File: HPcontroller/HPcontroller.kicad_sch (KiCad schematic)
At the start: 35 parts, among them Q1 Q_Dual_NMOS_S1G1S2G2D2D2D1D1, U1 Adafruit_QTPY_ESP32-C3, U2 NCP81071B, U5 ER-OLED0.49-1_MODULE, U6 Adafruit_MAX31850, U7 Adafruit_QTPY_ESP32-C3

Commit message: design "finished" need to do bom and footprints and layout
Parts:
- removed C1: 10u, Capacitor_SMD:C_0805_2012Metric_Pad1.18x1.45mm_HandSolder, symbol Device:C
- removed C4: C, Capacitor_SMD:C_0805_2012Metric_Pad1.18x1.45mm_HandSolder, symbol Device:C
- removed D1: D, Diode_SMD:D_SMB_Handsoldering, symbol Device:D
- removed D_3V3_POW1, D_HEAT1, D_HOT1, D_PD_POW1, D_RUN1: LED, LED_SMD:LED_0603_1608Metric_Pad1.05x0.95mm_HandSolder, symbol Device:LED
- removed Q1: Q_Dual_NMOS_S1G1S2G2D2D2D1D1, Package_SO:SOIC-8_3.9x4.9mm_P1.27mm, symbol Device:Q_Dual_NMOS_S1G1S2G2D2D2D1D1
- removed R1, R5, R6, R8: 100, Resistor_SMD:R_0805_2012Metric_Pad1.20x1.40mm_HandSolder, symbol Device:R
- removed R10, R7: 10k, Resistor_SMD:R_0805_2012Metric_Pad1.20x1.40mm_HandSolder, symbol Device:R
- removed R11: R, connector_custom:AMASS_XT60PW-M, symbol Device:R
- removed R14: 4k7, Resistor_SMD:R_0805_2012Metric_Pad1.20x1.40mm_HandSolder, symbol Device:R
- removed R4: 1k5, Resistor_SMD:R_0805_2012Metric_Pad1.20x1.40mm_HandSolder, symbol Device:R
- removed R9: 0, Jumper:SolderJumper-2_P1.3mm_Bridged_RoundedPad1.0x1.5mm, symbol Device:R
- removed SWDEC1, SWINC1, SWRST1, SWRUN1: SW_SPST, Button_Switch_SMD:SW_SPST_PTS645, symbol Switch:SW_SPST
- removed SWMODE1: SW_SPDT, Button_Switch_THT:SW_Slide_1P2T_CK_OS102011MS2Q, symbol Switch:SW_SPDT
- removed U1: Adafruit_QTPY_ESP32-C3, DevBoards:QTPY ESP32 C3, symbol DevBoards:Adafruit_QTPY_ESP32-C3
- removed U2: NCP81071B, Package_SO:SOIC-8_3.9x4.9mm_P1.27mm, symbol project_assorted:NCP81071B
- removed U5: ER-OLED0.49-1_MODULE, Connector_PinSocket_2.54mm:PinSocket_1x04_P2.54mm_Vertical, symbol DevBoards:ER-OLED0.49-1_MODULE
- removed U6: Adafruit_MAX31850, Connector_PinSocket_2.54mm:PinSocket_1x08_P2.54mm_Vertical, symbol DevBoards:Adafruit_MAX31850
- added J1: AudioJack4_Ground, symbol Connector_Audio:AudioJack4_Ground
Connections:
- net +3V3: now also J1.R2
- net GND: now also J1.S
- net SCL: now also U7.6 (SCL), J1.R1
- net SDA: now also U7.5 (SDA), J1.T
- net HEAT_DRIVE: now reaches U7.1 (A0)
- net SEL_A: now reaches U7.3 (A2)
- net SEL_B: now reaches U7.4 (A3)
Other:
- added sheet Controlpad (Controlpad.kicad_sch)
- added sheet Temperature Measurement System (Tmeas.kicad_sch)
- sheet HEATER DRIVE ports: added ENABLE_HEATER_DRIVE, HEATER FET DRIVE; removed none
- sheet ThermalProtector ports: added none; removed THM_PROT_RES
- note removed: "R11 is an xt60 to another board"
- moved on the sheet: H1, H2, H3, H4, R2, R3, U7

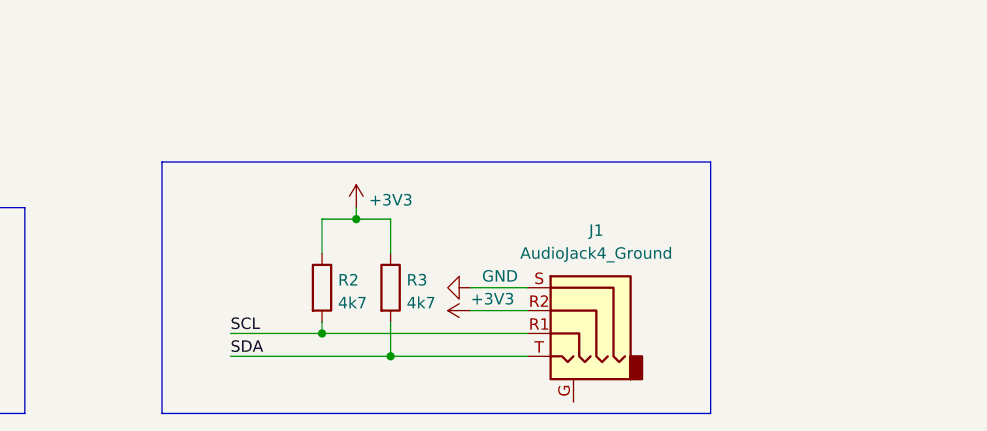
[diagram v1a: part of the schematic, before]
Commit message: started routing, finished footprintns
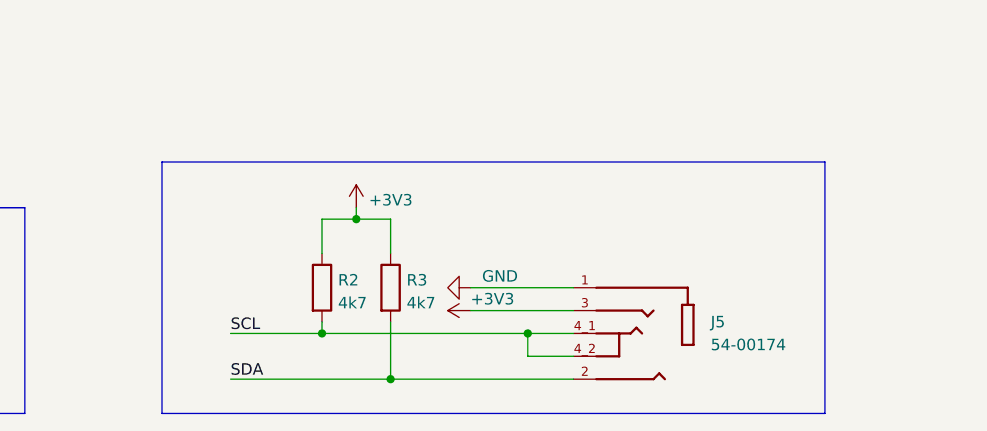
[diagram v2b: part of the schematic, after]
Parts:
- removed J1: AudioJack4_Ground, symbol Connector_Audio:AudioJack4_Ground
- added J5: 54-00174, TENSILITY_54-00174, symbol HPsym:54-00174
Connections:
- net +3V3: now also J5.3
- net GND: now also J5.1
- net SCL: now also J5.4_1, J5.4_2
- net SDA: now also J5.2
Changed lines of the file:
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@@
   (junction (at 105.41 171.45) (diameter 0) (color 0 0 0 0)
   )
-  (junction (at 109.22 186.69) (diameter 0) (color 0 0 0 0)
+  (junction (at 109.22 189.23) (diameter 0) (color 0 0 0 0)
+  )
+  (junction (at 124.46 184.15) (diameter 0) (color 0 0 0 0)
   )
   (junction (at 101.6 184.15) (diameter 0) (color 0 0 0 0)
@@
     (stroke (width 0) (type default))
   )
-  (wire (pts (xy 124.46 179.07) (xy 118.11 179.07))
+  (wire (pts (xy 118.11 179.07) (xy 129.54 179.07))
     (stroke (width 0) (type default))
   )
@@
     (stroke (width 0) (type default))
   )
+  (wire (pts (xy 124.46 186.69) (xy 124.46 184.15))
+    (stroke (width 0) (type default))
+  )
   (polyline (pts (xy 83.82 165.1) (xy 83.82 193.04))
     (stroke (width 0) (type default))
@@
     (stroke (width 0) (type default))
   )
+  (wire (pts (xy 124.46 184.15) (xy 129.54 184.15))
+    (stroke (width 0) (type default))
+  )
   (wire (pts (xy 101.6 175.26) (xy 101.6 171.45))
     (stroke (width 0) (type default))
   )
-  (wire (pts (xy 109.22 182.88) (xy 109.22 186.69))
-    (stroke (width 0) (type default))
-  )
   (polyline (pts (xy 68.58 193.04) (xy 21.59 193.04))
     (stroke (width 0) (type default))
@@
     (stroke (width 0) (type default))
   )
-  (wire (pts (xy 91.44 186.69) (xy 109.22 186.69))
-    (stroke (width 0) (type default))
-  )
-  (polyline (pts (xy 144.78 193.04) (xy 144.78 165.1))
+  (wire (pts (xy 91.44 189.23) (xy 109.22 189.23))
+    (stroke (width 0) (type default))
+  )
+  (polyline (pts (xy 157.48 193.04) (xy 157.48 165.1))
     (stroke (width 0) (type default))
   )
@@
     (stroke (width 0) (type default))
   )
-  (wire (pts (xy 109.22 186.69) (xy 124.46 186.69))
-    (stroke (width 0) (type default))
-  )
-  (polyline (pts (xy 83.82 165.1) (xy 144.78 165.1))
+  (wire (pts (xy 109.22 189.23) (xy 129.54 189.23))
+    (stroke (width 0) (type default))
+  )
+  (polyline (pts (xy 83.82 165.1) (xy 157.48 165.1))
     (stroke (width 0) (type default))
   )
@@
     (stroke (width 0) (type default))
   )
+  (wire (pts (xy 109.22 182.88) (xy 109.22 189.23))
+    (stroke (width 0) (type default))
+  )
   (wire (pts (xy 33.02 105.41) (xy 40.64 105.41))
     (stroke (width 0) (type default))
   )
-  (polyline (pts (xy 83.82 193.04) (xy 144.78 193.04))
+  (polyline (pts (xy 83.82 193.04) (xy 157.48 193.04))
+    (stroke (width 0) (type default))
+  )
+  (wire (pts (xy 129.54 186.69) (xy 124.46 186.69))
     (stroke (width 0) (type default))
   )
@@
     (stroke (width 0) (type default))
   )
-  (wire (pts (xy 118.11 181.61) (xy 124.46 181.61))
+  (wire (pts (xy 118.11 181.61) (xy 129.54 181.61))
     (stroke (width 0) (type default))
   )
@@
     (effects (font (size 1.27 1.27)) (justify left bottom))
   )
-  (label "SDA" (at 91.44 186.69 0) (fields_autoplaced)
+  (label "SDA" (at 91.44 189.23 0) (fields_autoplaced)
     (effects (font (size 1.27 1.27)) (justify left bottom))
   )
@@
         (path "/e63e39d7-6ac0-4ffd-8aa3-1841a4541b55"
           (reference "R2") (unit 1)
+        )
+      )
+    )
+  )
+  (symbol (lib_id "HPsym:54-00174") (at 137.16 184.15 0) (mirror y) (unit 1)
+    (in_bom yes) (on_board yes) (dnp no) (fields_autoplaced)
+    (property "Reference" "J5" (at 144.78 182.88 0)
+      (effects (font (size 1.27 1.27)) (justify right))
+    )
+    (property "Value" "54-00174" (at 144.78 185.42 0)
+      (effects (font (size 1.27 1.27)) (justify right))
+    )
+    (property "Footprint" "TENSILITY_54-00174" (at 138.43 173.99 0)
+      (effects (font (size 1.27 1.27)) (justify left bottom) hide)
+    )
+    (property "Datasheet" "" (at 137.16 184.15 0)
+      (effects (font (size 1.27 1.27)) (justify left bottom) hide)
+    )
+    (property "PARTREV" "A" (at 123.19 180.34 0)
+      (effects (font (size 1.27 1.27)) (justify left bottom) hide)
+    )
+    (property "STANDARD" "Manufacturer Recommendations" (at 138.43 176.53 0)
+      (effects (font (size 1.27 1.27)) (justify left bottom) hide)
+    )
+    (property "SNAPEDA_PN" "54-00174" (at 118.11 173.99 0)
+      (effects (font (size 1.27 1.27)) (justify left bottom) hide)
+    )
+    (property "MAXIMUM_PACKAGE_HEIGHT" "6mm" (at 121.92 180.34 0)
+      (effects (font (size 1.27 1.27)) (justify left bottom) hide)
+    )
+    (property "MANUFACTURER" "TENSILITY" (at 120.65 182.88 0)
+      (effects (font (size 1.27 1.27)) (justify left bottom) hide)
+    )
+    (property "MPN" "54-00174" (at 137.16 184.15 0)
+      (effects (font (size 1.27 1.27)) hide)
+    )
+    (pin "1")
+    (pin "2")
+    (pin "3")
+    (pin "4_1")
+    (pin "4_2")
+    (instances
+      (project "HPcontroller"
+        (path "/e63e39d7-6ac0-4ffd-8aa3-1841a4541b55"
+          (reference "J5") (unit 1)
         )
       )
@@
         )
       )
-    )
-  )
-  (symbol (lib_id "Connector_Audio:AudioJack4_Ground") (at 129.54 181.61 0) (mirror y) (unit 1)
-    (in_bom yes) (on_board yes) (dnp no)
-    (property "Reference" "J1" (at 132.08 172.72 0)
-      (effects (font (size 1.27 1.27)))
-    )
-    (property "Value" "AudioJack4_Ground" (at 132.08 175.26 0)
-      (effects (font (size 1.27 1.27)))
-    )
-    (property "Footprint" "" (at 129.54 181.61 0)
-      (effects (font (size 1.27 1.27)) hide)
-    )
-    (property "Datasheet" "~" (at 129.54 181.61 0)
-      (effects (font (size 1.27 1.27)) hide)
-    )
-    (pin "G")
-    (pin "R1")
-    (pin "R2")
-    (pin "S")
-    (pin "T")
-    (instances
-      (project "HPcontroller"
-        (path "/e63e39d7-6ac0-4ffd-8aa3-1841a4541b55"
-          (reference "J1") (unit 1)
-        )
-      )

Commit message: finished routing, moving on to heater
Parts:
- H1, H2, H3, H4: footprint MountingHole:MountingHole_3.2mm_M3_ISO14580 -> MountingHole:MountingHole_2.7mm_M2.5
- U7: footprint DevBoards:QTPY ESP32 C3 -> HPfootprint:QTPY ESP32 C3
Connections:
- net +3V3: now also U7.12 (3v3)
- net GND: now also U7.13 (GND)
- net SEL_A: now also U7.4 (A3); no longer U7.3 (A2)
- net SEL_B: now also U7.3 (A2); no longer U7.4 (A3)
- net INTA: now reaches U7.10 (MISO)
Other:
- sheet Controlpad ports: added INTA, SCL, SDA; removed none
- moved on the sheet: U7
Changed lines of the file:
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@@
+    (stroke (width 0) (type default))
+  )
+  (wire (pts (xy 53.34 105.41) (xy 59.69 105.41))
     (stroke (width 0) (type default))
   )
@@
     (stroke (width 0) (type default))
   )
-  (wire (pts (xy 33.02 102.87) (xy 40.64 102.87))
+  (wire (pts (xy 22.86 107.95) (xy 30.48 107.95))
     (stroke (width 0) (type default))
   )
@@
     (stroke (width 0) (type default))
   )
-  (wire (pts (xy 26.67 97.79) (xy 40.64 97.79))
+  (wire (pts (xy 16.51 102.87) (xy 30.48 102.87))
     (stroke (width 0) (type default))
   )
@@
     (stroke (width 0) (type default))
   )
+  (wire (pts (xy 171.45 101.6) (xy 177.8 101.6))
+    (stroke (width 0) (type default))
+  )
   (polyline (pts (xy 68.58 193.04) (xy 21.59 193.04))
     (stroke (width 0) (type default))
   )
+  (wire (pts (xy 171.45 99.06) (xy 177.8 99.06))
+    (stroke (width 0) (type default))
+  )
   (wire (pts (xy 87.63 139.7) (xy 93.98 139.7))
     (stroke (width 0) (type default))
@@
     (stroke (width 0) (type default))
   )
+  (wire (pts (xy 53.34 113.03) (xy 60.96 113.03))
+    (stroke (width 0) (type default))
+  )
   (wire (pts (xy 80.01 115.57) (xy 93.98 115.57))
     (stroke (width 0) (type default))
@@
     (stroke (width 0) (type default))
   )
-  (wire (pts (xy 33.02 105.41) (xy 40.64 105.41))
+  (wire (pts (xy 22.86 110.49) (xy 30.48 110.49))
     (stroke (width 0) (type default))
   )
@@
     (stroke (width 0) (type default))
   )
+  (wire (pts (xy 171.45 104.14) (xy 177.8 104.14))
+    (stroke (width 0) (type default))
+  )
   (wire (pts (xy 129.54 186.69) (xy 124.46 186.69))
     (stroke (width 0) (type default))
@@
     (stroke (width 0) (type default))
   )
-  (wire (pts (xy 34.29 107.95) (xy 40.64 107.95))
+  (wire (pts (xy 24.13 113.03) (xy 30.48 113.03))
     (stroke (width 0) (type default))
   )
@@
     (stroke (width 0) (type default))
   )
-  (wire (pts (xy 34.29 110.49) (xy 40.64 110.49))
+  (wire (pts (xy 55.88 107.95) (xy 53.34 107.95))
+    (stroke (width 0) (type default))
+  )
+  (wire (pts (xy 24.13 115.57) (xy 30.48 115.57))
     (stroke (width 0) (type default))
   )
@@
     (stroke (width 0) (type default))
   )
-  (label "SEL_B" (at 33.02 105.41 0) (fields_autoplaced)
+  (label "SCL" (at 171.45 101.6 0) (fields_autoplaced)
+    (effects (font (size 1.27 1.27)) (justify left bottom))
+  )
+  (label "SEL_B" (at 22.86 107.95 0) (fields_autoplaced)
     (effects (font (size 1.27 1.27)) (justify left bottom))
   )
@@
     (effects (font (size 1.27 1.27)) (justify left bottom))
   )
-  (label "HEAT_DRIVE" (at 27.94 97.79 0) (fields_autoplaced)
-    (effects (font (size 1.27 1.27)) (justify left bottom))
-  )
-  (label "SDA" (at 34.29 107.95 0) (fields_autoplaced)
-    (effects (font (size 1.27 1.27)) (justify left bottom))
-  )
-  (label "SCL" (at 34.29 110.49 0) (fields_autoplaced)
+  (label "HEAT_DRIVE" (at 17.78 102.87 0) (fields_autoplaced)
+    (effects (font (size 1.27 1.27)) (justify left bottom))
+  )
+  (label "SDA" (at 171.45 99.06 0) (fields_autoplaced)
+    (effects (font (size 1.27 1.27)) (justify left bottom))
+  )
+  (label "SDA" (at 24.13 113.03 0) (fields_autoplaced)
+    (effects (font (size 1.27 1.27)) (justify left bottom))
+  )
+  (label "SCL" (at 24.13 115.57 0) (fields_autoplaced)
+    (effects (font (size 1.27 1.27)) (justify left bottom))
+  )
+  (label "INTA" (at 171.45 104.14 0) (fields_autoplaced)
     (effects (font (size 1.27 1.27)) (justify left bottom))
   )
@@
     (effects (font (size 1.27 1.27)) (justify left bottom))
   )
-  (label "SEL_A" (at 33.02 102.87 0) (fields_autoplaced)
+  (label "SEL_A" (at 22.86 110.49 0) (fields_autoplaced)
     (effects (font (size 1.27 1.27)) (justify left bottom))
   )
@@
     (effects (font (size 1.27 1.27)) (justify left bottom))
   )
+  (label "INTA" (at 54.61 113.03 0) (fields_autoplaced)
+    (effects (font (size 1.27 1.27)) (justify left bottom))
+  )
   (symbol (lib_id "Mechanical:MountingHole") (at 30.48 182.88 0) (unit 1)
     (in_bom yes) (on_board yes) (dnp no) (fields_autoplaced)
@@
       (effects (font (size 1.27 1.27)) (justify left))
     )
-    (property "Footprint" "MountingHole:MountingHole_3.2mm_M3_ISO14580" (at 30.48 182.88 0)
+    (property "Footprint" "MountingHole:MountingHole_2.7mm_M2.5" (at 30.48 182.88 0)
       (effects (font (size 1.27 1.27)) hide)
     )
@@
     )
   )
+  (symbol (lib_id "power:GND") (at 59.69 105.41 90) (unit 1)
+    (in_bom yes) (on_board yes) (dnp no)
+    (property "Reference" "#PWR039" (at 66.04 105.41 0)
+      (effects (font (size 1.27 1.27)) hide)
+    )
+    (property "Value" "GND" (at 64.1334 105.41 90)
+      (effects (font (size 1.27 1.27)))
+    )
+    (property "Footprint" "" (at 59.69 105.41 0)
+      (effects (font (size 1.27 1.27)) hide)
+    )
+    (property "Datasheet" "" (at 59.69 105.41 0)
+      (effects (font (size 1.27 1.27)) hide)
+    )
+    (pin "1")
+    (instances
+      (project "HPcontroller"
+        (path "/e63e39d7-6ac0-4ffd-8aa3-1841a4541b55"
+          (reference "#PWR039") (unit 1)
+        )
+        (path "/e63e39d7-6ac0-4ffd-8aa3-1841a4541b55/2576b983-b407-4bb3-870d-6fa0fab97bf4"
+          (reference "#PWR059") (unit 1)
+        )
+      )
+    )
+  )
   (symbol (lib_id "Mechanical:MountingHole") (at 30.48 176.53 0) (unit 1)
     (in_bom yes) (on_board yes) (dnp no) (fields_autoplaced)
@@
       (effects (font (size 1.27 1.27)) (justify left))
     )
-    (property "Footprint" "MountingHole:MountingHole_3.2mm_M3_ISO14580" (at 30.48 176.53 0)
+    (property "Footprint" "MountingHole:MountingHole_2.7mm_M2.5" (at 30.48 176.53 0)
       (effects (font (size 1.27 1.27)) hide)
     )
@@
     )
   )
-  (symbol (lib_id "DevBoards:Adafruit_QTPY_ESP32-C3") (at 52.07 97.79 0) (unit 1)
-    (in_bom yes) (on_board yes) (dnp no) (fields_autoplaced)
-    (property "Reference" "U7" (at 52.07 92.871 0)
+  (symbol (lib_id "DevBoards:Adafruit_QTPY_ESP32-C3") (at 41.91 102.87 0) (unit 1)
+    (in_bom yes) (on_board yes) (dnp no) (fields_autoplaced)
+    (property "Reference" "U7" (at 41.91 97.951 0)
       (effects (font (size 1.27 1.27)))
     )
-    (property "Value" "Adafruit_QTPY_ESP32-C3" (at 52.07 95.4079 0)
+    (property "Value" "Adafruit_QTPY_ESP32-C3" (at 41.91 100.4879 0)
       (effects (font (size 1.27 1.27)))
     )
-    (property "Footprint" "DevBoards:QTPY ESP32 C3" (at 40.64 97.79 0)
-      (effects (font (size 1.27 1.27)) hide)
-    )
-    (property "Datasheet" "" (at 40.64 97.79 0)
+    (property "Footprint" "HPfootprint:QTPY ESP32 C3" (at 30.48 102.87 0)
+      (effects (font (size 1.27 1.27)) hide)
+    )
+    (property "Datasheet" "" (at 30.48 102.87 0)
       (effects (font (size 1.27 1.27)) hide)
     )
@@
     )
   )
+  (symbol (lib_id "power:+3V3") (at 55.88 107.95 270) (unit 1)
+    (in_bom yes) (on_board yes) (dnp no)
+    (property "Reference" "#PWR058" (at 52.07 107.95 0)
+      (effects (font (size 1.27 1.27)) hide)
+    )
+    (property "Value" "+3V3" (at 60.96 107.95 90)
+      (effects (font (size 1.27 1.27)))
+    )
+    (property "Footprint" "" (at 55.88 107.95 0)
+      (effects (font (size 1.27 1.27)) hide)
+    )
+    (property "Datasheet" "" (at 55.88 107.95 0)
+      (effects (font (size 1.27 1.27)) hide)
+    )
+    (pin "1")
+    (instances
+      (project "HPcontroller"
+        (path "/e63e39d7-6ac0-4ffd-8aa3-1841a4541b55/2576b983-b407-4bb3-870d-6fa0fab97bf4"
+          (reference "#PWR058") (unit 1)
+        )
+        (path "/e63e39d7-6ac0-4ffd-8aa3-1841a4541b55"
+          (reference "#PWR012") (unit 1)
+        )
+      )
+    )
+  )
   (symbol (lib_id "power:+3V3") (at 105.41 170.18 0) (unit 1)
     (in_bom yes) (on_board yes) (dnp no) (fields_autoplaced)
@@
       (effects (font (size 1.27 1.27)) (justify left))
     )
-    (property "Footprint" "MountingHole:MountingHole_3.2mm_M3_ISO14580" (at 48.26 182.88 0)
+    (property "Footprint" "MountingHole:MountingHole_2.7mm_M2.5" (at 48.26 182.88 0)
       (effects (font (size 1.27 1.27)) hide)
     )
@@
       (effects (font (size 1.27 1.27)) (justify left))
     )
-    (property "Footprint" "MountingHole:MountingHole_3.2mm_M3_ISO14580" (at 48.26 176.53 0)
+    (property "Footprint" "MountingHole:MountingHole_2.7mm_M2.5" (at 48.26 176.53 0)
       (effects (font (size 1.27 1.27)) hide)
     )
@@
       (effects (font (size 1.27 1.27)) (justify left top))
     )
-    (instances
+    (pin "SCL" input (at 177.8 101.6 180)
+      (effects (font (size 1.27 1.27)) (justify left))
+    )
+    (pin "SDA" input (at 177.8 99.06 180)
+      (effects (font (size 1.27 1.27)) (justify left))
+    )
+    (pin "INTA" input (at 177.8 104.14 180)
+      (effects (font (size 1.27 1.27)) (justify left))
+    )
+    (instances
